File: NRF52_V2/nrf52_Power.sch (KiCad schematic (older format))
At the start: 39 parts

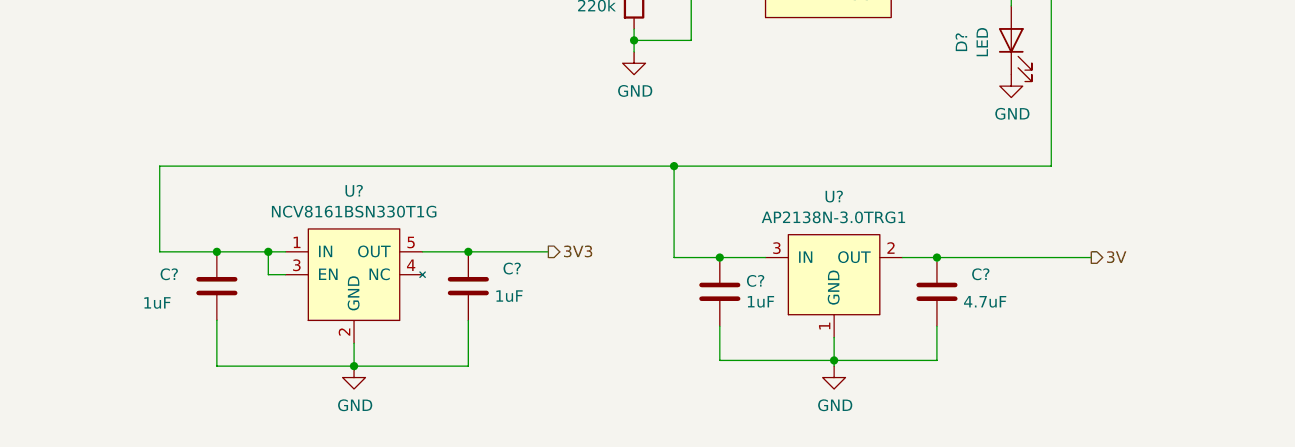
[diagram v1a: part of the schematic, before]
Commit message: Added SWD header and some buttons
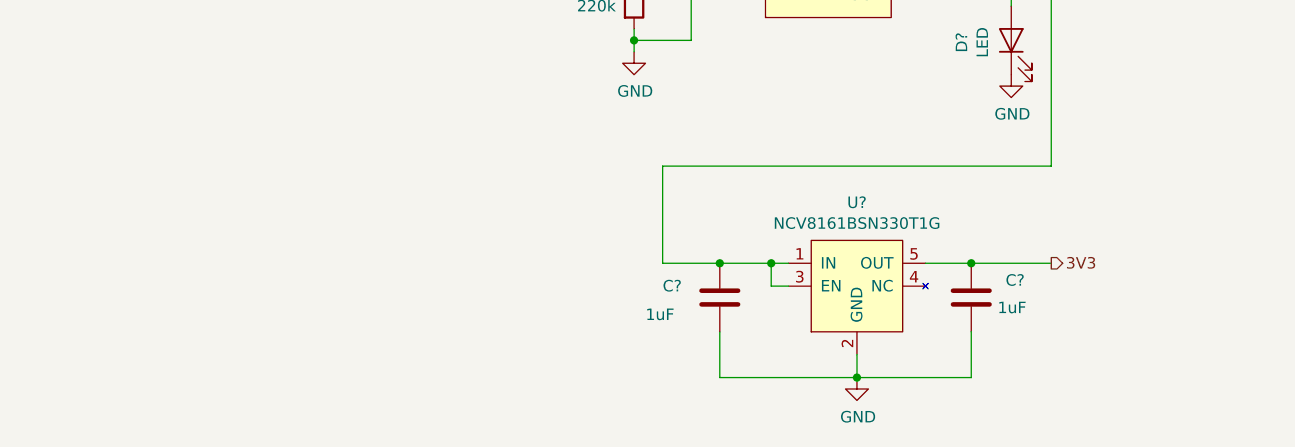
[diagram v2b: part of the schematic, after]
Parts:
- removed C?: 4.7uF, Capacitor_SMD:C_0603_1608Metric_Pad1.05x0.95mm_HandSolder, symbol Device:C
- removed C?: 1uF, Capacitor_SMD:C_0603_1608Metric_Pad1.05x0.95mm_HandSolder, symbol Device:C
- removed U?: AP2138N-3.0TRG1, Package_TO_SOT_SMD:SOT-23, symbol NRF52832_Reference-rescue:AP2138N-3.0TRG1-Project_Libary
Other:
- moved on the sheet: C?, U?
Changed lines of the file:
@@
 L Device:C C?
 U 1 1 5BF5917C
-P 1325 7025
+P 3525 7075
 AR Path="/5BF5917C" Ref="C?"  Part="1"
 AR Path="/5BF31556/5BF5917C" Ref="C?"  Part="1"
 AR Path="/5C31A75C/5BF5917C" Ref="C?"  Part="1"
-F 0 "C?" H 1075 7075 50  0000 L CNN
-F 1 "1uF" H 1000 6950 50  0000 L CNN
-F 2 "Capacitor_SMD:C_0603_1608Metric_Pad1.05x0.95mm_HandSolder" H 1363 6875 50  0001 C CNN
-F 3 "~" H 1325 7025 50  0001 C CNN
-	1    1325 7025
+F 0 "C?" H 3275 7125 50  0000 L CNN
+F 1 "1uF" H 3200 7000 50  0000 L CNN
+F 2 "Capacitor_SMD:C_0603_1608Metric_Pad1.05x0.95mm_HandSolder" H 3563 6925 50  0001 C CNN
+F 3 "~" H 3525 7075 50  0001 C CNN
+	1    3525 7075
 	1    0    0    -1
 $EndComp
@@
 L power:GND #PWR?
 U 1 1 5BF5918A
-P 1925 7375
+P 4125 7425
 AR Path="/5BF5918A" Ref="#PWR?"  Part="1"
 AR Path="/5BF31556/5BF5918A" Ref="#PWR?"  Part="1"
 AR Path="/5C31A75C/5BF5918A" Ref="#PWR?"  Part="1"
-F 0 "#PWR?" H 1925 7125 50  0001 C CNN
-F 1 "GND" H 1930 7202 50  0000 C CNN
-F 2 "" H 1925 7375 50  0001 C CNN
-F 3 "" H 1925 7375 50  0001 C CNN
-	1    1925 7375
+F 0 "#PWR?" H 4125 7175 50  0001 C CNN
+F 1 "GND" H 4130 7252 50  0000 C CNN
+F 2 "" H 4125 7425 50  0001 C CNN
+F 3 "" H 4125 7425 50  0001 C CNN
+	1    4125 7425
 	1    0    0    -1
 $EndComp
@@
 Wire Wire Line
 	2400 4650 2400 4450
-Text HLabel 2775 6875 2    50   Output ~ 0
+Text HLabel 4975 6925 2    50   Output ~ 0
 3V3
 Text HLabel 5400 5100 2    50   Output ~ 0
@@
 L Device:C C?
 U 1 1 5BF59183
-P 2425 7025
+P 4625 7075
 AR Path="/5BF59183" Ref="C?"  Part="1"
 AR Path="/5BF31556/5BF59183" Ref="C?"  Part="1"
 AR Path="/5C31A75C/5BF59183" Ref="C?"  Part="1"
-F 0 "C?" H 2575 7100 50  0000 L CNN
-F 1 "1uF" H 2540 6980 50  0000 L CNN
-F 2 "Capacitor_SMD:C_0603_1608Metric_Pad1.05x0.95mm_HandSolder" H 2463 6875 50  0001 C CNN
-F 3 "~" H 2425 7025 50  0001 C CNN
-	1    2425 7025
+F 0 "C?" H 4775 7150 50  0000 L CNN
+F 1 "1uF" H 4740 7030 50  0000 L CNN
+F 2 "Capacitor_SMD:C_0603_1608Metric_Pad1.05x0.95mm_HandSolder" H 4663 6925 50  0001 C CNN
+F 3 "~" H 4625 7075 50  0001 C CNN
+	1    4625 7075
 	1    0    0    -1
 $EndComp
@@
 Wire Wire Line
 	4800 5250 4800 5100
-Connection ~ 1925 7375
-Wire Wire Line
-	1925 7275 1925 7375
+Connection ~ 4125 7425
+Wire Wire Line
+	4125 7325 4125 7425
 Wire Notes Line
 	7300 500  7300 6525
@@
 	4975 5100 4975 6500
 $Comp
-L NRF52832_Reference-rescue:AP2138N-3.0TRG1-Project_Libary U?
-U 1 1 5C11B1D5
-P 4025 6900
-AR Path="/5C11B1D5" Ref="U?"  Part="1"
-AR Path="/5BF31556/5C11B1D5" Ref="U?"  Part="1"
-AR Path="/5C31A75C/5C11B1D5" Ref="U?"  Part="1"
-F 0 "U?" H 4025 7165 50  0000 C CNN
-F 1 "AP2138N-3.0TRG1" H 4025 7074 50  0000 C CNN
-F 2 "Package_TO_SOT_SMD:SOT-23" H 4025 7150 50  0001 C CNN
-F 3 "" H 4025 7150 50  0001 C CNN
-	1    4025 6900
-	1    0    0    -1
-$EndComp
-$Comp
-L Device:C C?
-U 1 1 5C11B374
-P 4475 7050
-AR Path="/5C11B374" Ref="C?"  Part="1"
-AR Path="/5BF31556/5C11B374" Ref="C?"  Part="1"
-AR Path="/5C31A75C/5C11B374" Ref="C?"  Part="1"
-F 0 "C?" H 4625 7125 50  0000 L CNN
-F 1 "4.7uF" H 4590 7005 50  0000 L CNN
-F 2 "Capacitor_SMD:C_0603_1608Metric_Pad1.05x0.95mm_HandSolder" H 4513 6900 50  0001 C CNN
-F 3 "~" H 4475 7050 50  0001 C CNN
-	1    4475 7050
-	1    0    0    -1
-$EndComp
-$Comp
-L Device:C C?
-U 1 1 5C11E4AB
-P 3525 7050
-F 0 "C?" H 3640 7096 50  0000 L CNN
-F 1 "1uF" H 3640 7005 50  0000 L CNN
-F 2 "Capacitor_SMD:C_0603_1608Metric_Pad1.05x0.95mm_HandSolder" H 3563 6900 50  0001 C CNN
-F 3 "~" H 3525 7050 50  0001 C CNN
-	1    3525 7050
-	1    0    0    -1
-$EndComp
-$Comp
-L power:GND #PWR?
-U 1 1 5C11E770
-P 4025 7375
-F 0 "#PWR?" H 4025 7125 50  0001 C CNN
-F 1 "GND" H 4030 7202 50  0000 C CNN
-F 2 "" H 4025 7375 50  0001 C CNN
-F 3 "" H 4025 7375 50  0001 C CNN
-	1    4025 7375
-	1    0    0    -1
-$EndComp
-Wire Wire Line
-	3525 7200 3525 7350
-Wire Wire Line
-	3525 7350 4025 7350
-Wire Wire Line
-	4025 7350 4025 7375
-Wire Wire Line
-	4025 7250 4025 7350
-Connection ~ 4025 7350
-Wire Wire Line
-	4475 7200 4475 7350
-Wire Wire Line
-	4475 7350 4025 7350
-Wire Wire Line
-	3725 6900 3525 6900
-Wire Wire Line
-	3325 6900 3325 6500
-Connection ~ 3525 6900
-Wire Wire Line
-	3525 6900 3325 6900
-Wire Wire Line
-	4325 6900 4475 6900
-Connection ~ 4475 6900
-Wire Wire Line
-	4475 6900 5150 6900
-Text HLabel 5150 6900 2    50   Output ~ 0
-3V
-$Comp
 L Project_Libary:SLIDE_SW_DPDT U?
 U 1 1 5C1C929E
@@
 NoConn ~ 5700 1725
 NoConn ~ 5600 1725
-Connection ~ 3325 6500
-Wire Wire Line
-	3325 6500 4975 6500
-Wire Wire Line
-	1075 6500 3325 6500
 $Comp
 L Device:C C?
@@
 L Project_Libary:NCV8161BSN330T1G U?
 U 1 1 5C1429EA
-P 1925 6925
-F 0 "U?" H 1925 7240 50  0000 C CNN
-F 1 "NCV8161BSN330T1G" H 1925 7149 50  0000 C CNN
-F 2 "Package_SO:TSOP-5_1.65x3.05mm_P0.95mm" H 1825 7375 50  0001 C CNN
-F 3 "" H 1825 7375 50  0001 C CNN
-	1    1925 6925
-	1    0    0    -1
-$EndComp
-Connection ~ 2425 6875
-Wire Wire Line
-	2425 6875 2775 6875
-Wire Wire Line
-	1075 6500 1075 6875
-Wire Wire Line
-	1075 6875 1325 6875
-Connection ~ 1325 6875
-Wire Wire Line
-	1325 6875 1550 6875
-Wire Wire Line
-	1325 7175 1325 7375
-Wire Wire Line
-	1325 7375 1925 7375
-Wire Wire Line
-	2425 7375 2425 7175
-Wire Wire Line
-	1925 7375 2425 7375
-Wire Wire Line
-	2225 6875 2425 6875
-Wire Wire Line
-	1625 6975 1550 6975
-Wire Wire Line
-	1550 6975 1550 6875
-Connection ~ 1550 6875
-Wire Wire Line
-	1550 6875 1625 6875
+P 4125 6975
+F 0 "U?" H 4125 7290 50  0000 C CNN
+F 1 "NCV8161BSN330T1G" H 4125 7199 50  0000 C CNN
+F 2 "Package_SO:TSOP-5_1.65x3.05mm_P0.95mm" H 4025 7425 50  0001 C CNN
+F 3 "" H 4025 7425 50  0001 C CNN
+	1    4125 6975
+	1    0    0    -1
+$EndComp
+Connection ~ 4625 6925
+Wire Wire Line
+	4625 6925 4975 6925
+Wire Wire Line
+	3275 6925 3525 6925
+Connection ~ 3525 6925
+Wire Wire Line
+	3525 6925 3750 6925
+Wire Wire Line
+	3525 7225 3525 7425
+Wire Wire Line
+	3525 7425 4125 7425
+Wire Wire Line
+	4625 7425 4625 7225
+Wire Wire Line
+	4125 7425 4625 7425
+Wire Wire Line
+	4425 6925 4625 6925
+Wire Wire Line
+	3825 7025 3750 7025
+Wire Wire Line
+	3750 7025 3750 6925
+Connection ~ 3750 6925
+Wire Wire Line
+	3750 6925 3825 6925
 $Comp
 L Device:Fuse F?
@@
 	1800 2150 1550 2150
 Connection ~ 1550 2150
+Wire Wire Line
+	4975 6500 3275 6500
+Wire Wire Line
+	3275 6500 3275 6925
 $EndSCHEMATC
